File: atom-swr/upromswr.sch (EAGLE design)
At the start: 3 parts

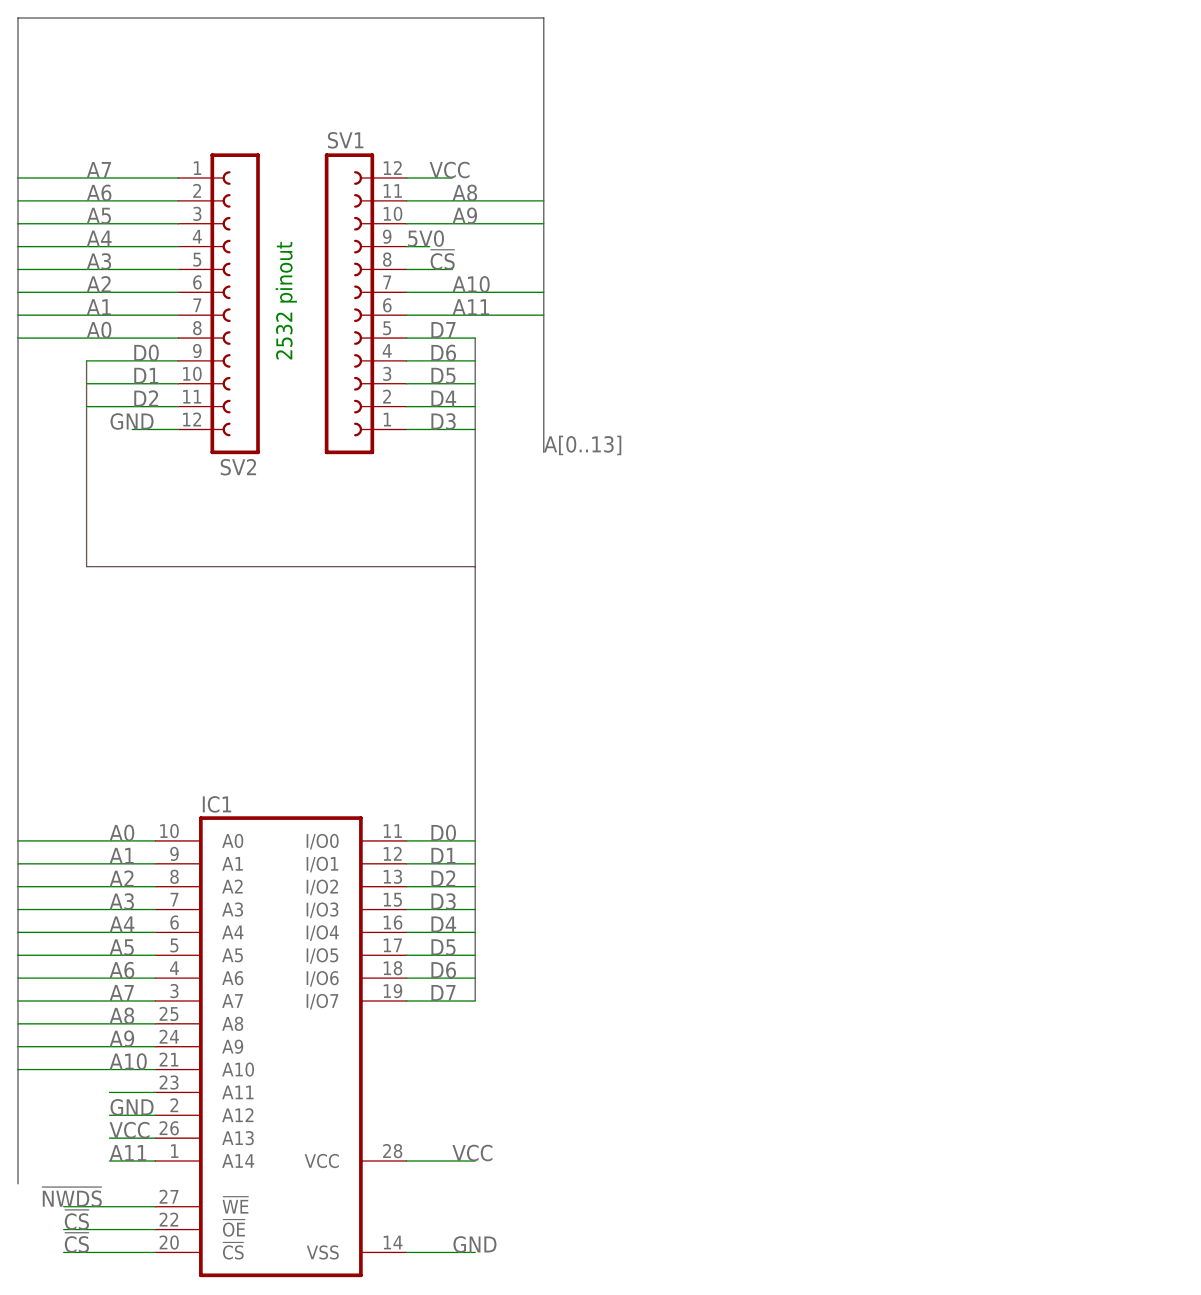
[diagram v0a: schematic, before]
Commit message: adding extender and swr notes
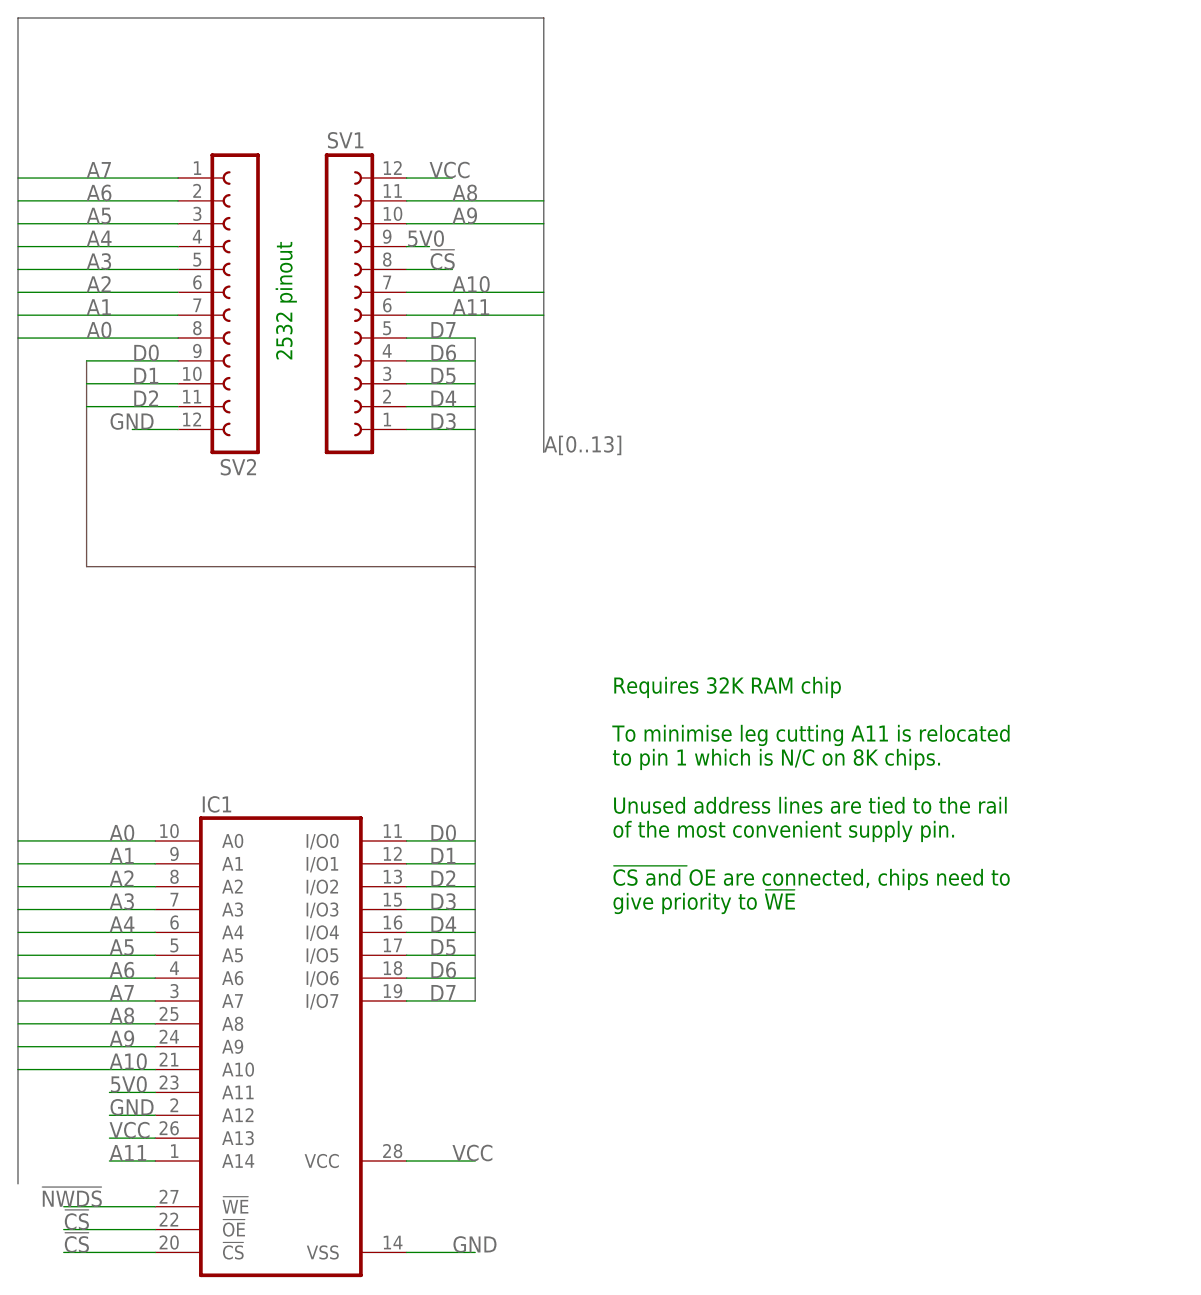
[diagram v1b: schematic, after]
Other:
- note added: "Requires 32K RAM chip To minimise leg cutting A11 is relocated to pin 1 which is N/C on 8K chips. Unused address lines are tied to the rail of the most convenient supply pin. !CS and !OE are connected, chips need to give priority to !WE"
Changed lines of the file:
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@@
 <?xml version="1.0" encoding="utf-8"?>
 <!DOCTYPE eagle SYSTEM "eagle.dtd">
-<eagle version="9.6.0">
+<eagle version="9.6.1">
 <drawing>
 <settings>
@@
 <plain>
 <text x="17.78" y="132.08" size="1.778" layer="91" rot="R90">2532 pinout</text>
+<text x="53.34" y="71.12" size="1.778" layer="91">Requires 32K RAM chip
+To minimise leg cutting A11 is relocated
+to pin 1 which is N/C on 8K chips.
+Unused address lines are tied to the rail
+of the most convenient supply pin.
+!CS and !OE are connected, chips need to
+give priority to !WE</text>
 </plain>
 <instances>
@@
 <pinref part="IC1" gate="G$1" pin="A11"/>
 <wire x1="2.54" y1="50.8" x2="-2.54" y2="50.8" width="0.1524" layer="91"/>
+<label x="-2.54" y="50.8" size="1.778" layer="95"/>
 </segment>
 </net>
@@
 </drawing>
 <compatibility>
+<note version="6.3" minversion="6.2.2" severity="warning">
+Since Version 6.2.2 text objects can contain more than one line,
+which will not be processed correctly with this version.
+</note>
 <note version="8.2" severity="warning">
 Since Version 8.2, EAGLE supports online libraries. The ids
